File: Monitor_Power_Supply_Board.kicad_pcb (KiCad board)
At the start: 2 copper layers, 77.7 x 47.7 mm, 12 parts, among them J1 Conn_01x02, J2 Conn_01x02, J3 Conn_01x02

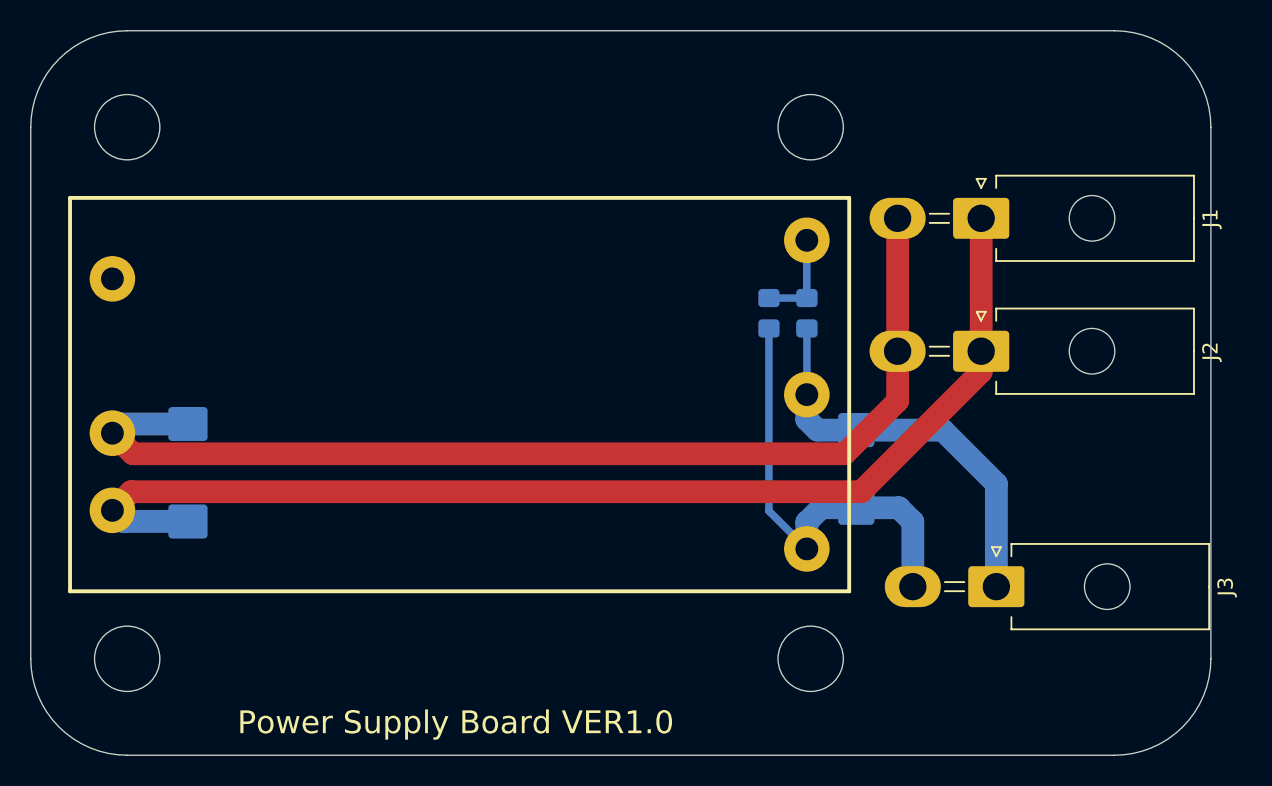
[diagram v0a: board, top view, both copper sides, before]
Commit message: VER1.0: добавил разъем для вентилятора и индикацию питания
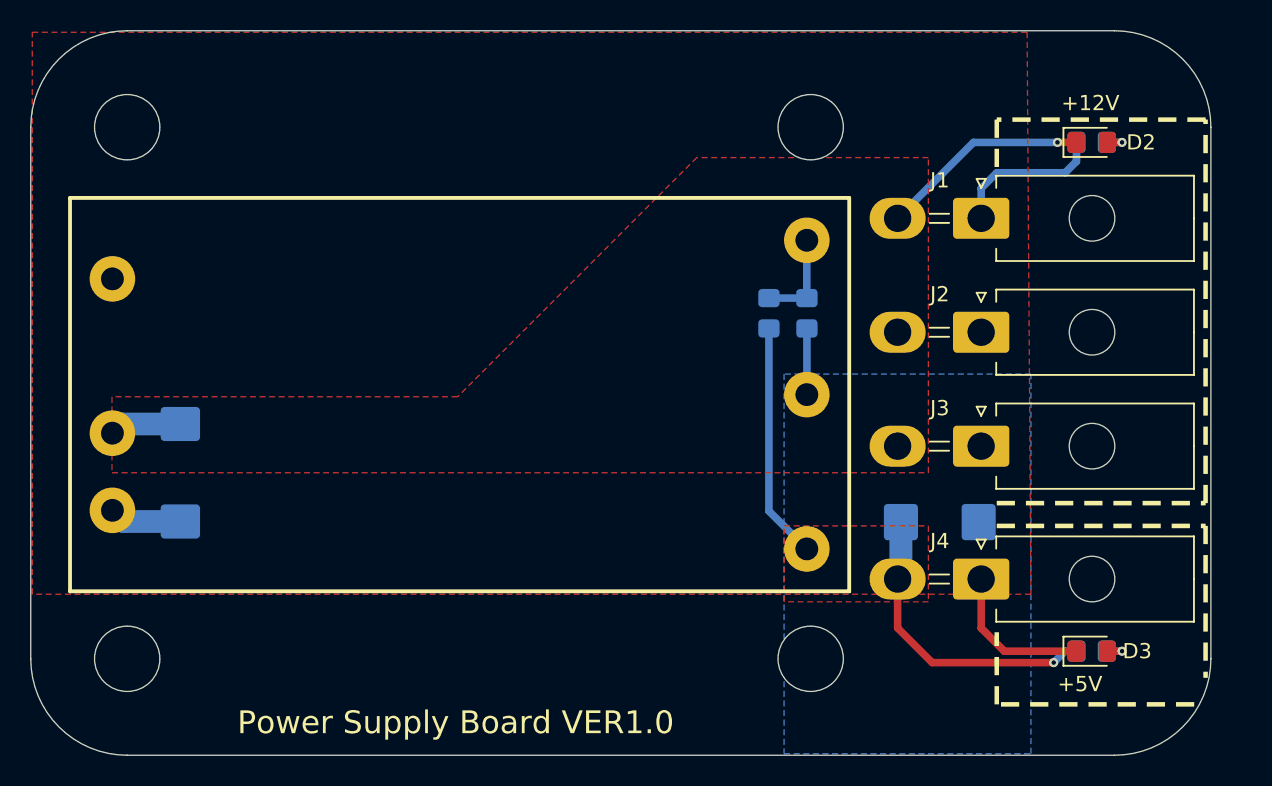
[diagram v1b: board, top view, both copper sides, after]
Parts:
- added D2: LED_Small, LED_SMD:LED_0805_2012Metric_Pad1.15x1.40mm_HandSolder, F.Cu at (170.7, 92.4)
- added D3: LED_Small, LED_SMD:LED_0805_2012Metric_Pad1.15x1.40mm_HandSolder, F.Cu at (170.7, 125.9)
- added J4: Conn_01x02, Connector_Molex:Molex_Mini-Fit_Jr_5569-02A2_2x01_P4.20mm_Horizontal, F.Cu at (163.5, 121.1)
- added R3: 2k, Resistor_SMD:R_0805_2012Metric_Pad1.20x1.40mm_HandSolder, B.Cu at (170.7, 92.4)
- added R4: 1k, Resistor_SMD:R_0805_2012Metric_Pad1.20x1.40mm_HandSolder, B.Cu at (170.7, 125.9)
- C1: value 220u -> 47u; footprint Capacitor_Tantalum_SMD:CP_EIA-6032-28_Kemet-C_HandSolder -> Capacitor_Tantalum_SMD:CP_EIA-7343-31_Kemet-D_HandSolder
- C2: value 47u -> 220u; footprint Capacitor_Tantalum_SMD:CP_EIA-7343-31_Kemet-D_HandSolder -> Capacitor_Tantalum_SMD:CP_EIA-6032-28_Kemet-C_HandSolder
- moved C2 49.6 mm to (160.7, 117.4), turned to 0 degrees
- moved C1 44.5 mm to (110.7, 114.1)
- moved J3 9.30 mm to (163.5, 112.4)
- moved J2 1.25 mm to (163.5, 104.9)
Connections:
- C1 pad 1: +5V -> VDD
- C1 pad 2: GND -> VSS
- C2 pad 1: VDD -> +5V
- C2 pad 2: VSS -> GND
- J3 pad 1: GND -> VDD
- J3 pad 2: +5V -> VSS
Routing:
- net VDD: track 76.4 -> 16.3 mm
- net VSS: track 70.9 -> 18.6 mm, vias 0 -> 1
- net GND: track 27.0 -> 14.5 mm
- net +5V: track 29.3 -> 35.6 mm, vias 0 -> 1
- net Net-(D3-A): track 0.00 -> 1.97 mm, vias 0 -> 1
- net Net-(D2-A): track 0.00 -> 1.97 mm, vias 0 -> 1
- added copper zone on F.Cu, net +5V
- added copper zone on B.Cu, net GND
- added copper zone on F.Cu, net VDD
- added copper zone on F.Cu, net VSS
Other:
- board text added: "+12V"
- board text added: "+5V"
